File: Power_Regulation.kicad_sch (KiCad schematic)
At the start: 67 parts, among them J12 Conn_01x02, J13 Conn_02x01, J14 Conn_02x01, K1 G5Q-1A DC24, Q3 BSS138, Q3 DMP6023LE-13, Q4 BSS138, U10 TLC555xPS, U11 TPS78450QDBVRQ1, U12 LM66200DRLR, U7 LM3880-1AA, U8 LMR33630BDDA, U9 TPS78533QKVURQ1

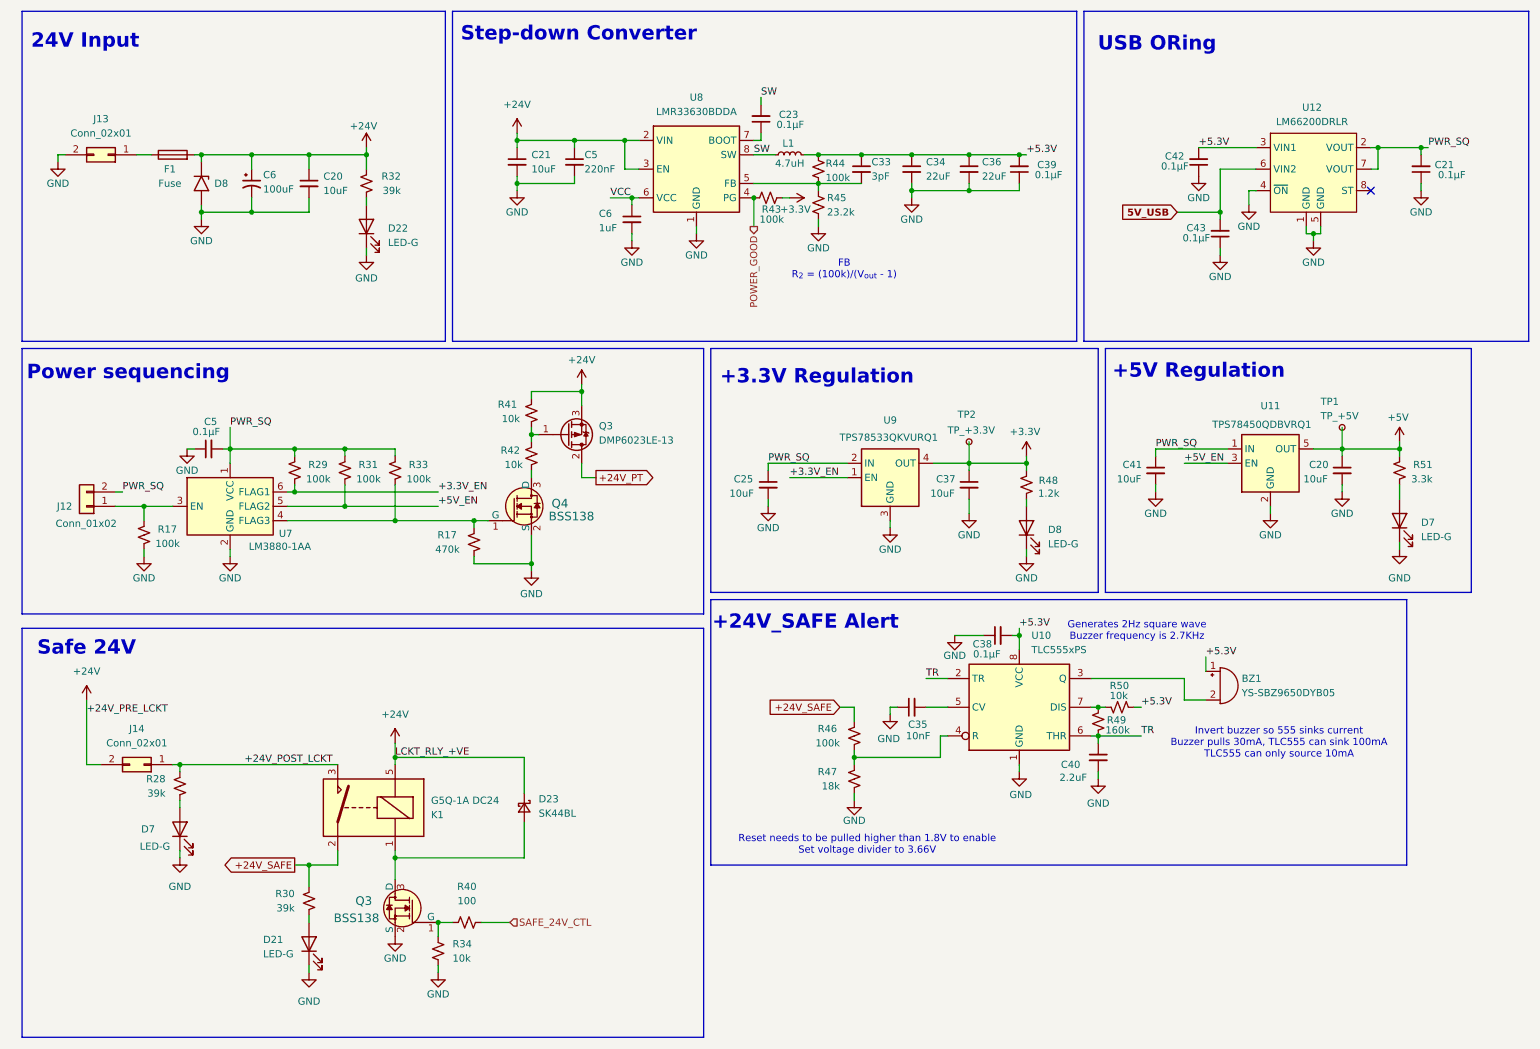
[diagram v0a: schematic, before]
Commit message: Updated to 4-pin fans, moved power pages together, deleted old reference.
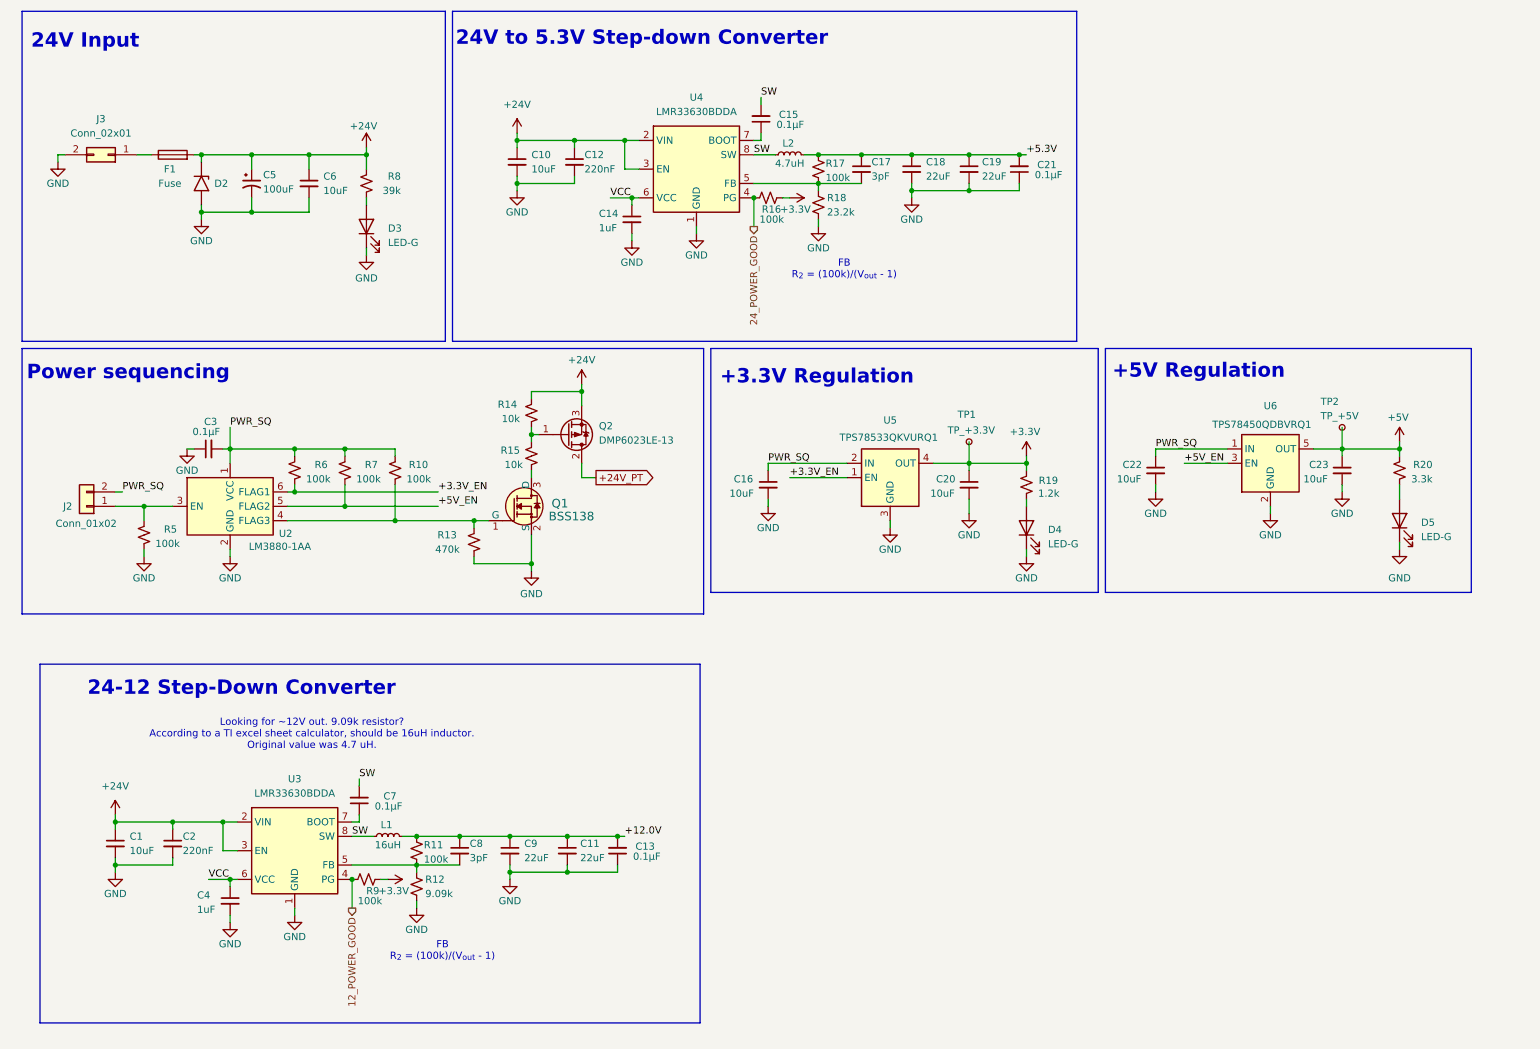
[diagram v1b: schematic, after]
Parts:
- removed BZ1: YS-SBZ9650DYB05, Library:YS-SBZ9650DYB05, symbol Device:Buzzer
- removed C21, C38, C42, C43: 0.1μF, Capacitor_SMD:C_0402_1005Metric, symbol Device:C_Small
- removed C35: 10nF, Capacitor_SMD:C_0402_1005Metric, symbol Device:C_Small
- removed C40: 2.2uF, Capacitor_SMD:C_0603_1608Metric, symbol Device:C_Small
- removed D21, D7: LED-G, LED_SMD:LED_0805_2012Metric, symbol Device:LED
- removed D23: SK44BL, Diode_SMD:D_SMB, symbol Device:D_Schottky_Small
- removed J14: Conn_02x01, Connector_Molex:Molex_Mini-Fit_Jr_5566-02A_2x01_P4.20mm_Vertical, symbol Connector_Generic:Conn_02x01
- removed K1: G5Q-1A DC24, Relay_THT:Relay_SPST_Omron-G5Q-1A, symbol Relay:G5Q-1A
- removed Q3: BSS138, Package_TO_SOT_SMD:SOT-23-3, symbol dk_Transistors-FETs-MOSFETs-Single:BSS138
- removed R28, R30: 39k, Resistor_SMD:R_0402_1005Metric, symbol Device:R_Small_US
- removed R34, R50: 10k, Resistor_SMD:R_0402_1005Metric, symbol Device:R_Small_US
- removed R40: 100, Resistor_SMD:R_0402_1005Metric, symbol Device:R_Small_US
- removed R46: 100k, Resistor_SMD:R_0603_1608Metric, symbol Device:R_Small_US
- removed R47: 18k, Resistor_SMD:R_0603_1608Metric, symbol Device:R_Small_US
- removed R49: 160k, Resistor_SMD:R_0402_1005Metric, symbol Device:R_Small_US
- removed U10: TLC555xPS, Package_SO:VSSOP-8_3x3mm_P0.65mm, symbol Timer:TLC555xPS
- removed U12: LM66200DRLR, Package_TO_SOT_SMD:SOT-583-8, symbol LM66200DRLR:LM66200DRLR
- added C1: 10uF, Capacitor_SMD:C_1206_3216Metric, symbol Device:C_Small
- added C11, C9: 22uF, Capacitor_SMD:C_0805_2012Metric, symbol Device:C_Small
- added C13, C7: 0.1μF, Capacitor_SMD:C_0402_1005Metric, symbol Device:C_Small
- added C2: 220nF, Capacitor_SMD:C_0805_2012Metric, symbol Device:C_Small
- added C4: 1uF, Capacitor_SMD:C_0603_1608Metric, symbol Device:C_Small
- added C8: 3pF, Capacitor_SMD:C_0603_1608Metric, symbol Device:C_Small
- added L1: 16uH, Inductor_SMD:L_Bourns_SRP7028A_7.3x6.6mm, symbol Device:L_Small
- added R11, R9: 100k, Resistor_SMD:R_0603_1608Metric, symbol Device:R_Small_US
- added R12: 9.09k, Resistor_SMD:R_0603_1608Metric, symbol Device:R_Small_US
- added U3: LMR33630BDDA, Package_SO:Texas_HSOP-8-1EP_3.9x4.9mm_P1.27mm_ThermalVias, symbol Regulator_Switching:LMR33630BDDA
- renumbered C21 to C10, C5 to C12, C6 to C14, C23 to C15, C25 to C16, C33 to C17, C34 to C18, C36 to C19, C37 to C20, C39 to C21, C41 to C22, C20 to C23, C5 to C3, C6 to C5, C20 to C6, D8 to D2, D22 to D3, D8 to D4, D7 to D5, J12 to J2, J13 to J3, L1 to L2, Q4 to Q1, Q3 to Q2, R33 to R10, R17 to R13, R41 to R14, R42 to R15, R43 to R16, R44 to R17, R45 to R18, R48 to R19, R51 to R20, R17 to R5, R29 to R6, R31 to R7, R32 to R8, TP2 to TP1, TP1 to TP2, U7 to U2, U8 to U4, U9 to U5, U11 to U6
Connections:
- net +24V: now also C1.1, C2.1, U3.2 (VIN), U3.3 (EN)
- net +3.3V: now also R9.2
- net GND: now also C1.2, C11.2, C13.1, C2.2, C4.2, C9.2, R12.2, U3.1 (GND), U3.9 (GND)
- net SW: now also C7.2, L1.1, U3.8 (SW)
- net VCC: now also C4.1, U3.6 (VCC)
- net POWER_GOOD renamed 24_POWER_GOOD
- new net: C8.2, R11.2, R12.1, U3.5 (FB)
- new net: C7.1, U3.7 (BOOT)
- new net +12.0V: C11.1, C13.2, C8.1, C9.1, L1.2, R11.1
- new net 12_POWER_GOOD: R9.1, U3.4 (PG)
- no-connect marks 1 -> 0
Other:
- note added: "24-12 Step-Down Converter"
- note added: "24V to 5.3V Step-down Converter"
- note added: "Looking for ~12V out. 9.09k resistor? According to a TI excel sheet calculator, should be 16uH inductor. Original value was 4.7 uH."
- note removed: "+24V_SAFE Alert"
- note removed: "Generates 2Hz square wave Buzzer frequency is 2.7KHz"
- note removed: "Invert buzzer so 555 sinks current Buzzer pulls 30mA, TLC555 can sink 100mA TLC555 can only source 10mA"
- note removed: "Reset needs to be pulled higher than 1.8V to enable Set voltage divider to 3.66V"
- note removed: "Safe 24V"
- note removed: "Step-down Converter"
- note removed: "USB ORing"

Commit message: Adopted 4-layer setup and organized placement
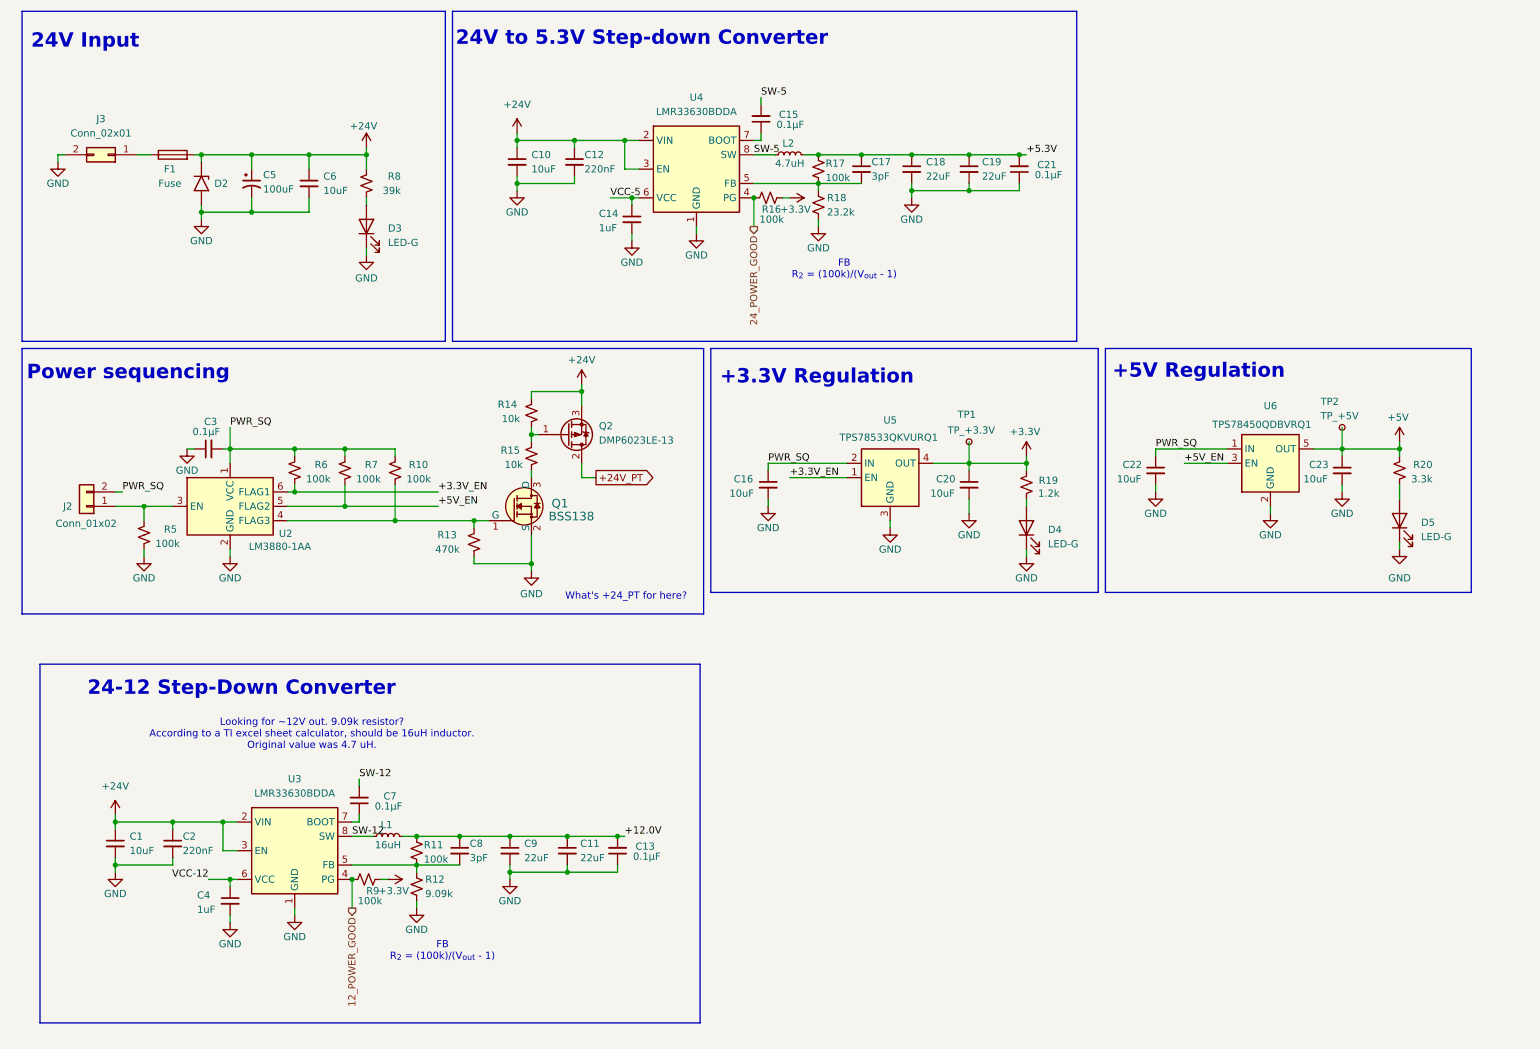
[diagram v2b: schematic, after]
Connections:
- net SW renamed SW-12
- net SW-12: no longer C15.2, L2.1, U4.8 (SW)
- net VCC renamed VCC-12
- net VCC-12: no longer C14.1, U4.6 (VCC)
- new net SW-5: C15.2, L2.1, U4.8 (SW)
- new net VCC-5: C14.1, U4.6 (VCC)
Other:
- note added: "What's +24_PT for here?"
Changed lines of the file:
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@@
+		)
+	)
+	(text "What's +24_PT for here?"
+		(exclude_from_sim no)
+		(at 119.634 118.872 0)
+		(effects
+			(font
+				(size 1.27 1.27)
+			)
 		)
 	)
@@
 		)
 	)
-	(label "SW"
+	(label "SW-12"
 		(at 71.12 161.29 0)
 		(effects
@@
 		)
 	)
-	(label "SW"
+	(label "SW-5"
 		(at 143.51 30.48 0)
 		(effects
@@
 		)
 	)
-	(label "SW"
+	(label "SW-12"
 		(at 72.39 151.13 0)
 		(effects
@@
 		)
 	)
-	(label "VCC"
-		(at 45.72 168.91 0)
+	(label "VCC-12"
+		(at 45.72 168.91 180)
 		(effects
 			(font
 				(size 1.27 1.27)
 			)
-			(justify left bottom)
+			(justify right bottom)
 		)
 	)
@@
 		)
 	)
-	(label "VCC"
+	(label "VCC-5"
 		(at 116.84 48.26 0)
 		(effects
@@
 		)
 	)
-	(label "SW"
+	(label "SW-5"
 		(at 142.24 40.64 0)
 		(effects

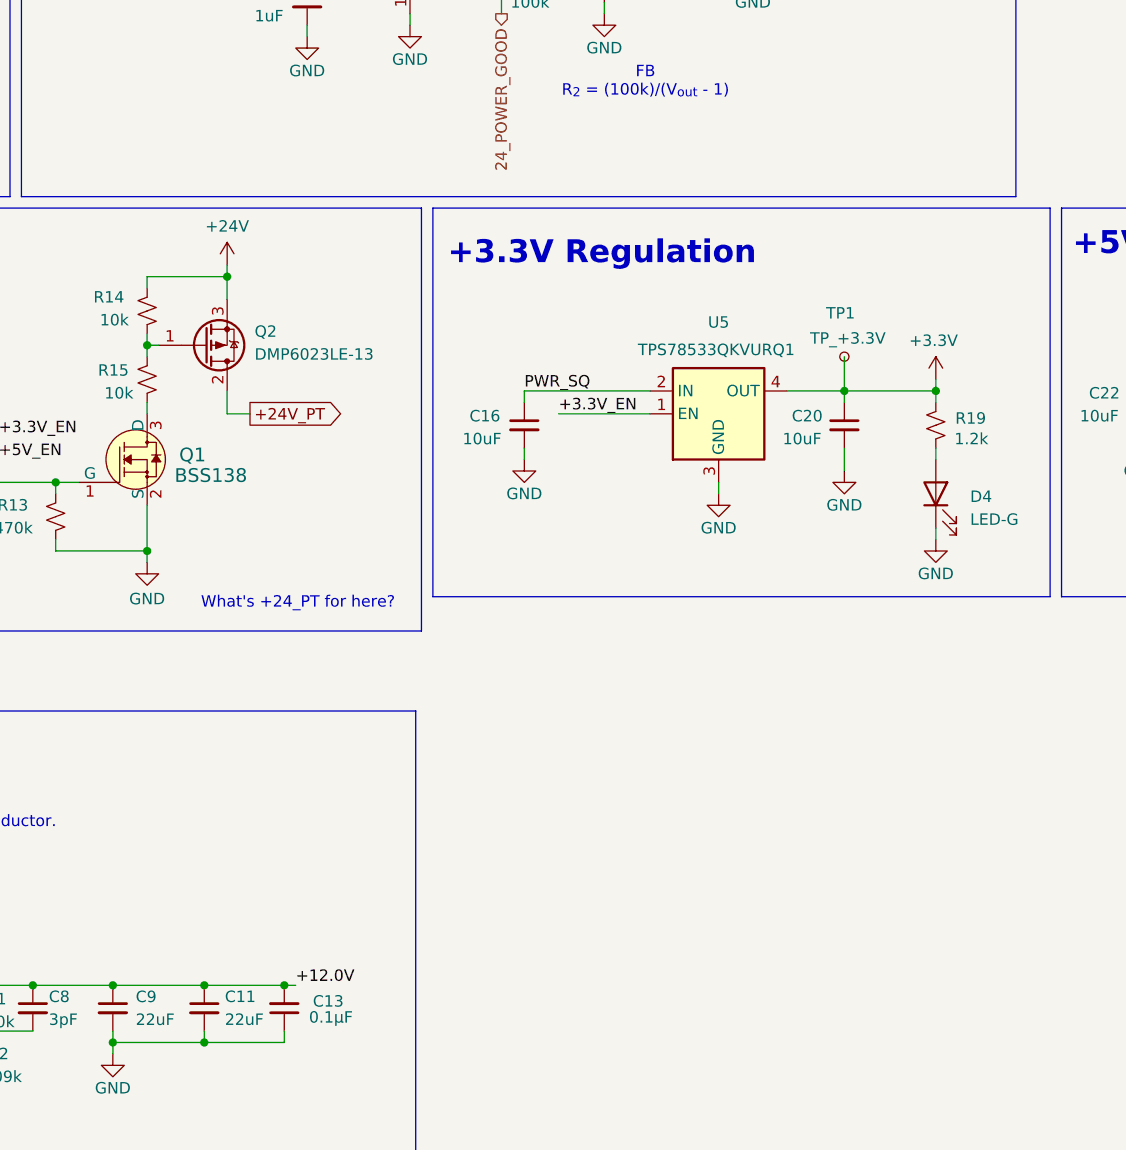
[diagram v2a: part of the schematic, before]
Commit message: Initial PCB placement and wiring.
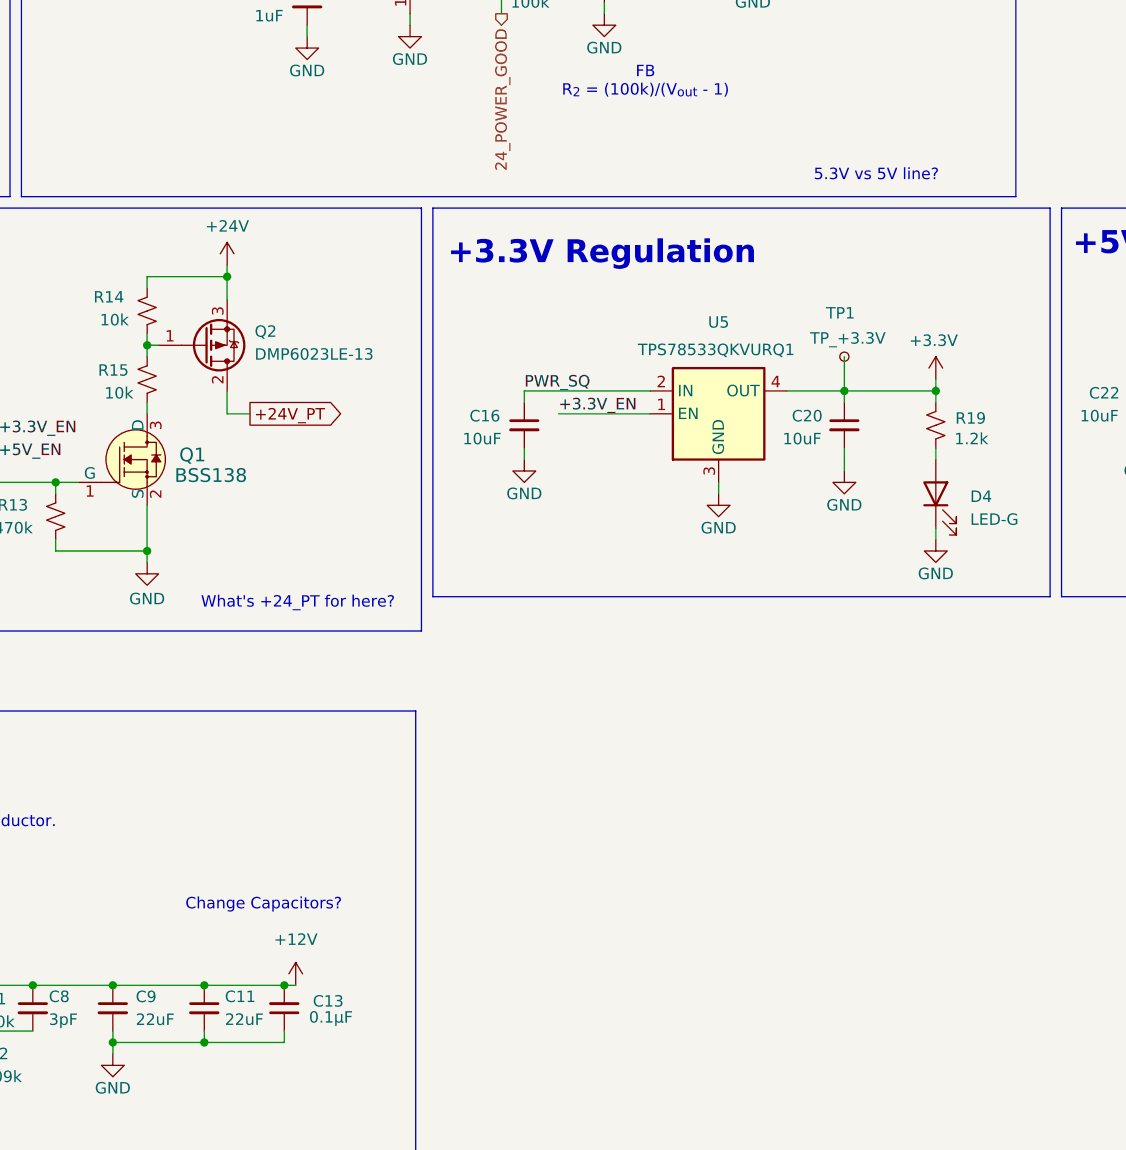
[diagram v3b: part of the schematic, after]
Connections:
- net +12.0V renamed +12V
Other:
- note added: "5.3V vs 5V line?"
- note added: "Change Capacitors?"
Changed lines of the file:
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@@
 		)
 	)
+	(text "5.3V vs 5V line?"
+		(exclude_from_sim no)
+		(at 183.896 71.374 0)
+		(effects
+			(font
+				(size 1.27 1.27)
+			)
+		)
+	)
 	(text "24V to 5.3V Step-down Converter"
 		(exclude_from_sim no)
@@
 		)
 	)
+	(text "Change Capacitors?\n"
+		(exclude_from_sim no)
+		(at 115.824 152.4 0)
+		(effects
+			(font
+				(size 1.27 1.27)
+			)
+		)
+	)
 	(text "Power sequencing"
 		(exclude_from_sim no)
@@
 		)
 	)
-	(label "+12.0V"
-		(at 119.38 161.29 0)
-		(effects
-			(font
-				(size 1.27 1.27)
-			)
-			(justify left bottom)
-		)
-	)
 	(label "SW-5"
 		(at 143.51 30.48 0)
@@
 					(unit 1)
 				)
+			)
+		)
+	)
+	(symbol
+		(lib_id "power:+12V")
+		(at 119.38 161.29 0)
+		(unit 1)
+		(exclude_from_sim no)
+		(in_bom yes)
+		(on_board yes)
+		(dnp no)
+		(fields_autoplaced yes)
+		(property "Reference" "#PWR02"
+			(at 119.38 165.1 0)
+			(effects
+				(font
+					(size 1.27 1.27)
+				)
+				(hide yes)
+			)
+		)
+		(property "Value" "+12V"
+			(at 119.38 156.21 0)
+			(effects
+				(font
+					(size 1.27 1.27)
+				)
+			)
+		)
+		(property "Footprint" ""
+			(at 119.38 161.29 0)
+			(effects
+				(font
+					(size 1.27 1.27)
+				)
+				(hide yes)
+			)
+		)
+		(property "Datasheet" ""
+			(at 119.38 161.29 0)
+			(effects
+				(font
+					(size 1.27 1.27)
+				)
+				(hide yes)
+			)
+		)
+		(property "Description" "Power symbol creates a global label with name \"+12V\""
+			(at 119.38 161.29 0)
+			(effects
+				(font
+					(size 1.27 1.27)
+				)
+				(hide yes)
+			)
+		)
+		(pin "1"
+		)
+		(instances
+			(project ""
+				(path "/24817451-dfe0-4b9a-9d93-7304529c9d58/ee31919e-6383-4dab-aec3-a18ec94a437b"
+					(reference "#PWR02")
+					(unit 1)
+				)

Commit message: Updated power regulation, To-Do: Rewire PCB
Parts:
- removed Q1: BSS138, Package_TO_SOT_SMD:SOT-23-3, symbol dk_Transistors-FETs-MOSFETs-Single:BSS138
- removed Q2: DMP6023LE-13, Package_TO_SOT_SMD:SOT-223-3_TabPin2, symbol Transistor_FET:ZXMP4A16G
- removed R13: 470k, Resistor_SMD:R_0603_1608Metric, symbol Device:R_Small_US
- removed R14, R15: 10k, Resistor_SMD:R_0402_1005Metric, symbol Device:R_Small_US
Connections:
- net PWR_SQ is gone; now on net +5.3V: C16.1, C22.1, C3.2, J2.2 (Pin_2), R10.2, R6.2, R7.2, U2.1 (VCC), U5.2 (IN), U6.1 (IN)
- net +24V: no longer U3.3 (EN)
- net +12_EN: now reaches R10.1, U2.4 (FLAG3)
- net +12_EN: now also U3.3 (EN)
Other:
- moved on the sheet: C1, C2
